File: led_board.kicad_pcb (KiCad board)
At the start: 2 copper layers, 193 parts, among them J1 SEAM-50-01-L-06-2-RA-GP-TR

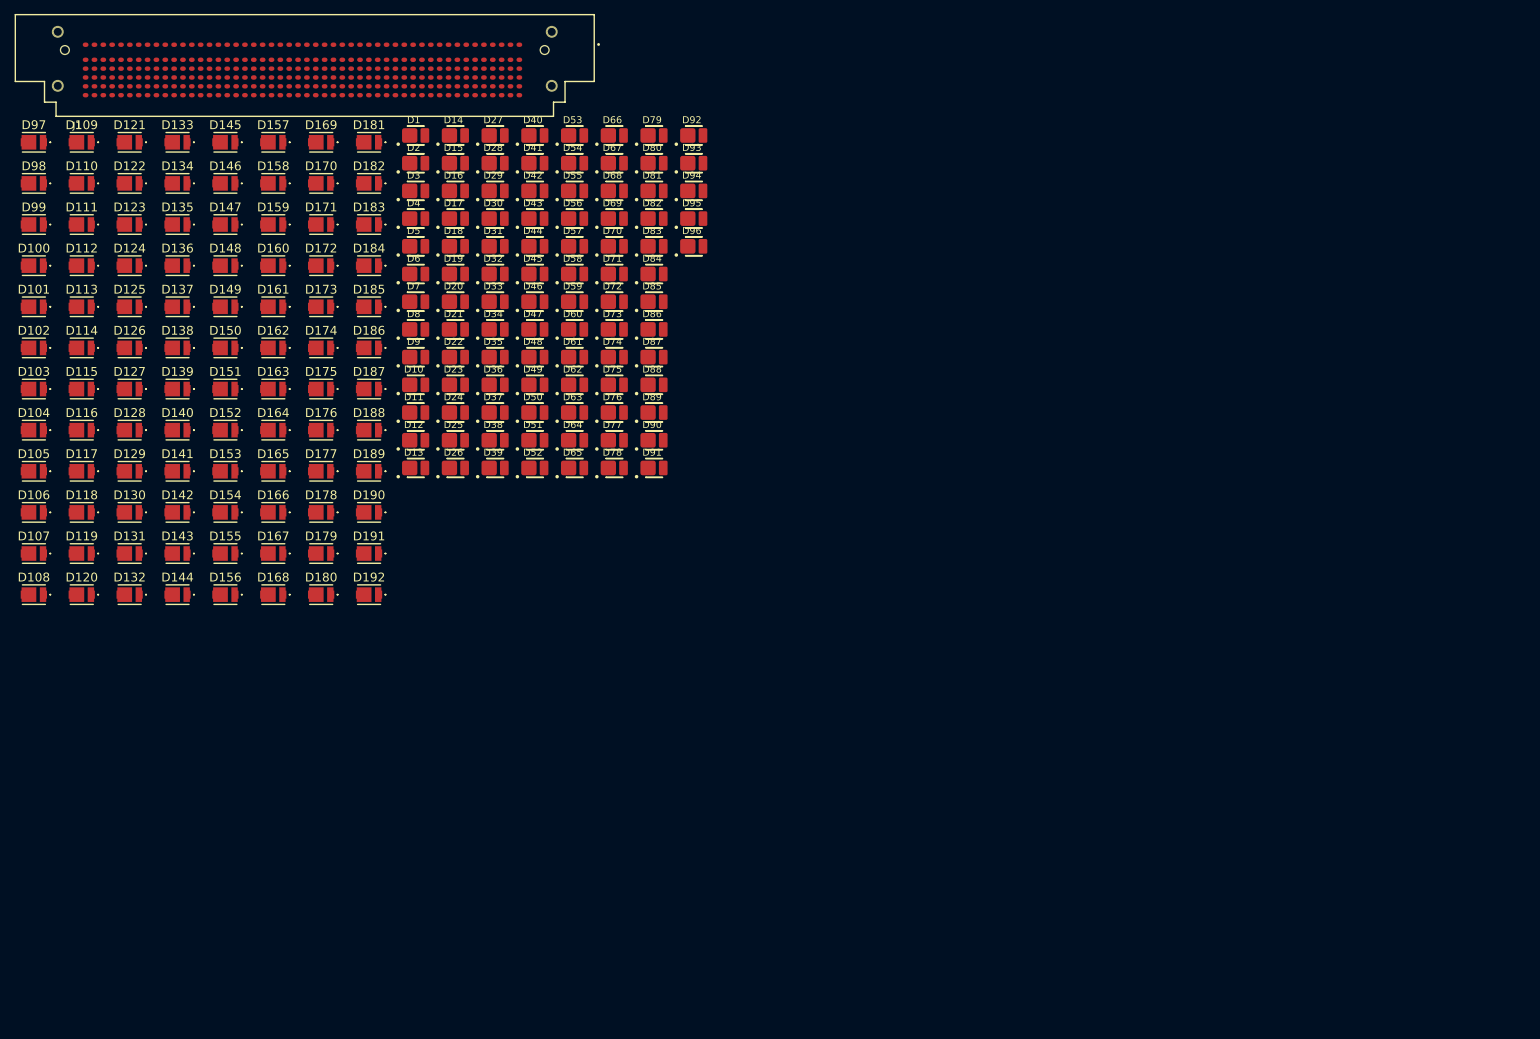
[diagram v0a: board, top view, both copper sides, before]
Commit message: first prod ver, with well plate mount
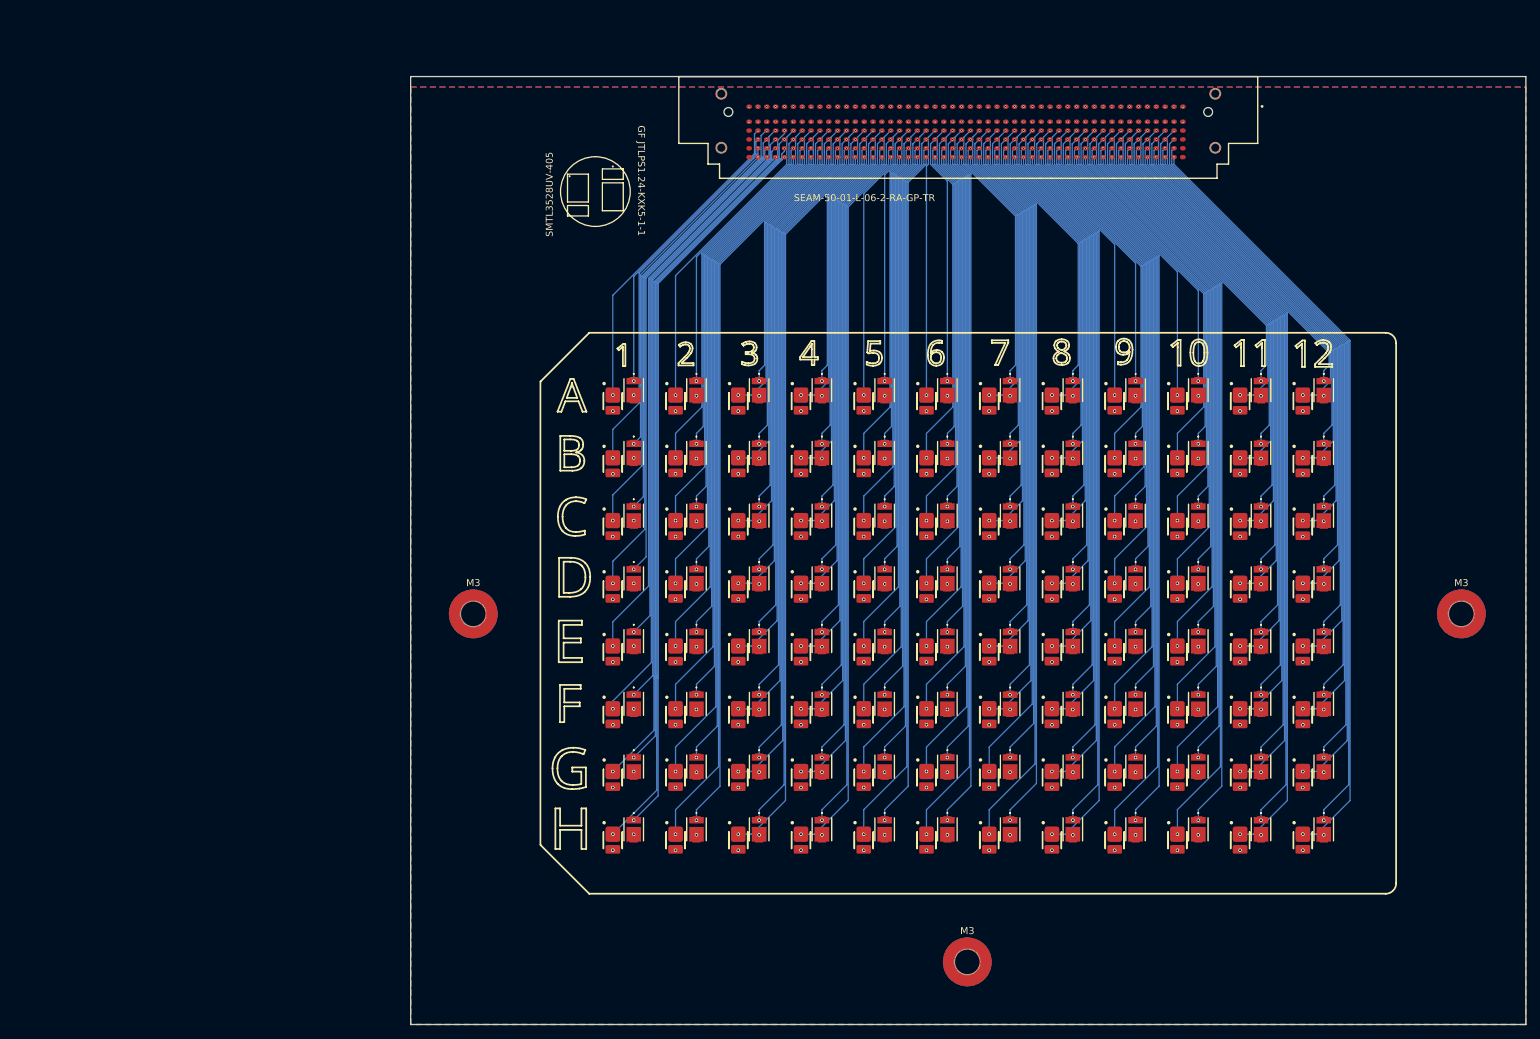
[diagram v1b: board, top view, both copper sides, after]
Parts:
- added M3: MountingHole_Pad, MountingHole:MountingHole_3.5mm_Pad_TopBottom, F.Cu at (85.0, 113.1)
- added M3: MountingHole_Pad, MountingHole:MountingHole_3.5mm_Pad_TopBottom, F.Cu at (155.9, 163.0)
- added M3: MountingHole_Pad, MountingHole:MountingHole_3.5mm_Pad_TopBottom, F.Cu at (226.7, 113.1)
- D100, D101, D102, D103, D104, D105, D106, D107, D108, D109, D110, D111, D112, D113, D114, D115, D116, D117, D118, D119, D120, D121, D122, D123, D124, D125, D126, D127, D128, D129, D130, D131, D132, D133, D134, D135, D136, D137, D138, D139, D140, D141, D142, D143, D144, D145, D146, D147, D148, D149, D150, D151, D152, D153, D154, D155, D156, D157, D158, D159, D160, D161, D162, D163, D164, D165, D166, D167, D168, D169, D170, D171, D172, D173, D174, D175, D176, D177, D178, D179, D180, D181, D182, D183, D184, D185, D186, D187, D188, D189, D190, D191, D192, D97, D98, D99: footprint LED_SMD:GFJTLPS124KXK511 -> GF_JTLP mod:GFJTLPS124KXK511
- moved D123 184.1 mm to (198.0, 144.0), turned to 90 degrees
- moved D99 183.2 mm to (198.0, 108.0), turned to 90 degrees
- moved D97 181.6 mm to (198.0, 90.0), turned to 90 degrees
- moved D121 181.2 mm to (198.0, 126.0), turned to 90 degrees
- moved D100 179.7 mm to (198.0, 99.0), turned to 90 degrees
- moved D98 178.5 mm to (198.0, 81.0), turned to 90 degrees
- moved D124 177.5 mm to (198.0, 135.0), turned to 90 degrees
- moved D104 176.6 mm to (189.0, 144.0), turned to 90 degrees
- moved D103 175.6 mm to (189.0, 135.0), turned to 90 degrees
- moved D122 175.1 mm to (198.0, 117.0), turned to 90 degrees
- moved D102 174.7 mm to (189.0, 126.0), turned to 90 degrees
- moved D101 173.8 mm to (189.0, 117.0), turned to 90 degrees
- moved D171 168.0 mm to (207.0, 144.0), turned to 90 degrees
- moved D147 165.6 mm to (207.0, 108.0), turned to 90 degrees
- moved D169 164.9 mm to (207.0, 126.0), turned to 90 degrees
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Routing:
- net /75A: track 0.00 -> 111.5 mm, vias 0 -> 2
- net /27A: track 0.00 -> 109.9 mm, vias 0 -> 2
- net /72A: track 0.00 -> 108.6 mm, vias 0 -> 2
- net /75B: track 0.00 -> 108.5 mm, vias 0 -> 2
- net /8A: track 0.00 -> 108.2 mm, vias 0 -> 2
- net /24A: track 0.00 -> 107.0 mm, vias 0 -> 2
- net /27B: track 0.00 -> 106.9 mm, vias 0 -> 2
- net /56A: track 0.00 -> 106.6 mm, vias 0 -> 2
- net /76A: track 0.00 -> 105.3 mm, vias 0 -> 2
- net /43A: track 0.00 -> 105.2 mm, vias 0 -> 2
- net /83A: track 0.00 -> 105.1 mm, vias 0 -> 2
- net /72B: track 0.00 -> 104.1 mm, vias 0 -> 2
- net /36A: track 0.00 -> 103.7 mm, vias 0 -> 2
- net /28A: track 0.00 -> 103.7 mm, vias 0 -> 2
- net /91A: track 0.00 -> 103.6 mm, vias 0 -> 2
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- added copper zone on In1.Cu, net /V_A
- added copper zone on In2.Cu, net /V_B
- added copper zone on B.Cu, net GND
- added copper zone on F.Cu, net GND
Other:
- board outline added: 160 x 136 mm
- copper layers 2 -> 4
- board text added: "GF JTLPS1.24-KXK5-1-1"
- board text added: "SMTL3528UV-405"

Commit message: pnp stuff
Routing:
- net /58B: track 41.4 -> 40.6 mm
- net /10B: track 39.7 -> 39.0 mm

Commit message: pnp stuff
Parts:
- added ?: , , F.Cu at (191.4, 46.2)
- added ?: , , F.Cu at (120.6, 38.5)
- added REF**: Untitled, Fiducials:Untitled, F.Cu at (120.6, 46.3)
